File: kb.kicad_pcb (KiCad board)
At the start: 2 copper layers, 110.5 x 91.4 mm, 67 parts, among them U4 HOLE

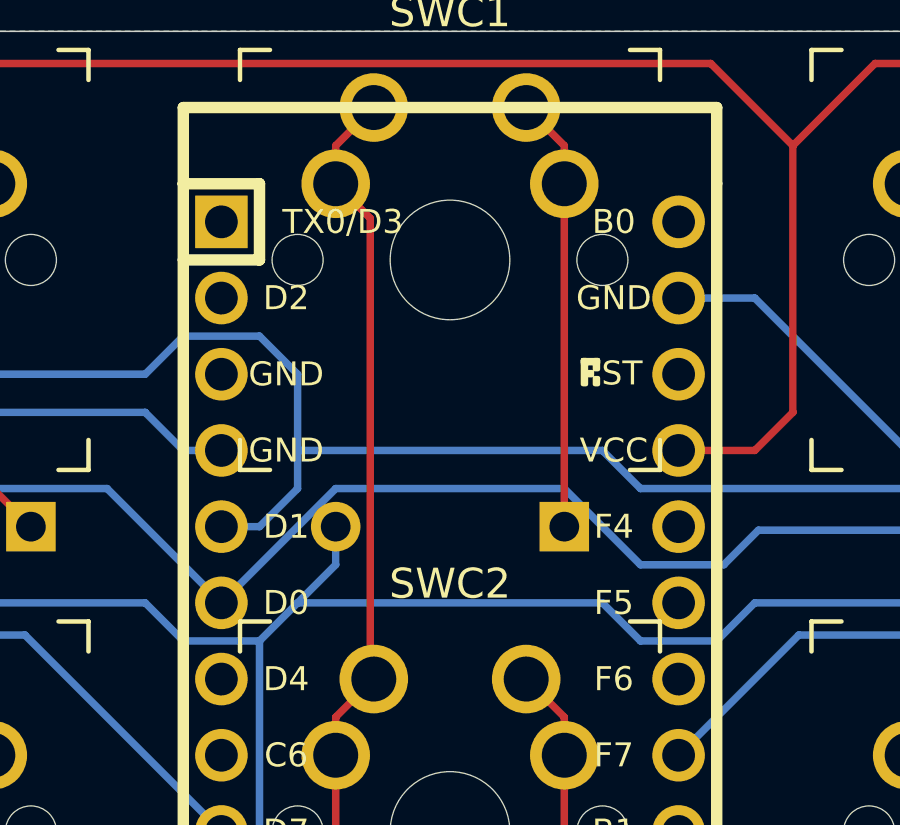
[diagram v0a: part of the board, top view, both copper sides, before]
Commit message: Fixed intersecting diode and trace (fixed #1)
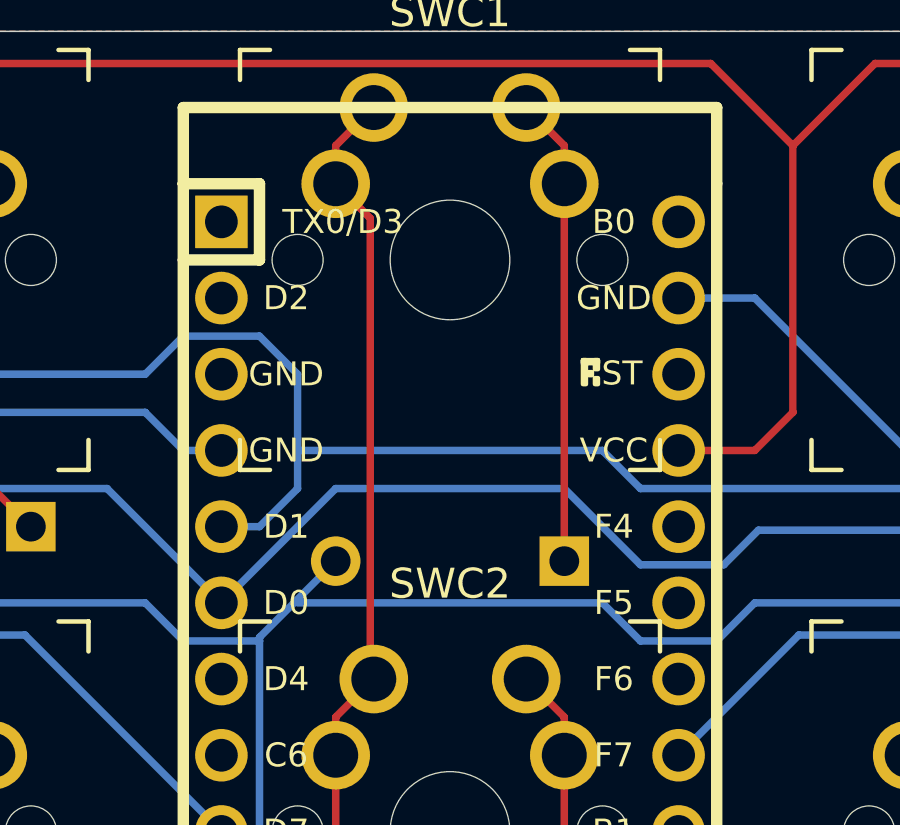
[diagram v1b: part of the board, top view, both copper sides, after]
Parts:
- moved D11 1.15 mm to (135.9, 71.0)
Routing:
- net Net-(D11-Pad2): track 14.5 -> 15.6 mm
- net Net-(D1-Pad1): track 120.3 -> 119.2 mm

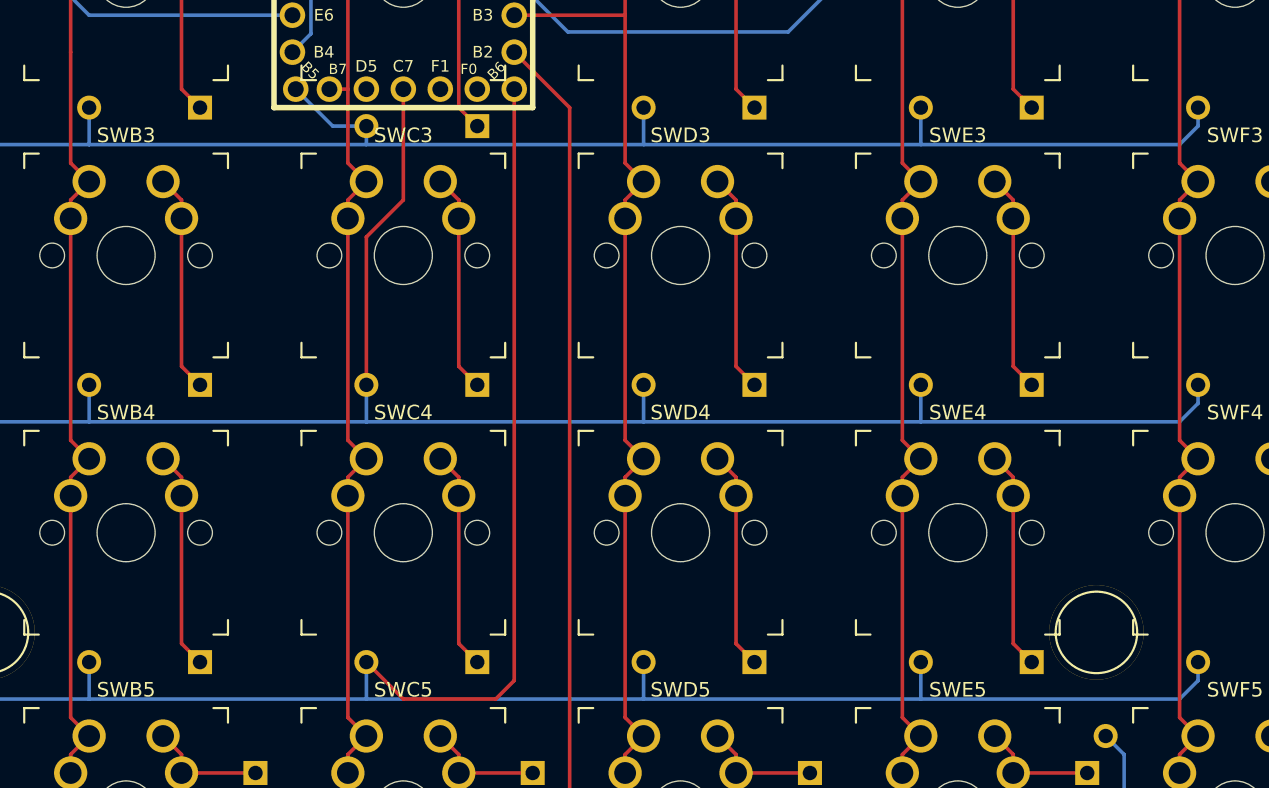
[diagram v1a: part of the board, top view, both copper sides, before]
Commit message: Shifted diode to improve fill
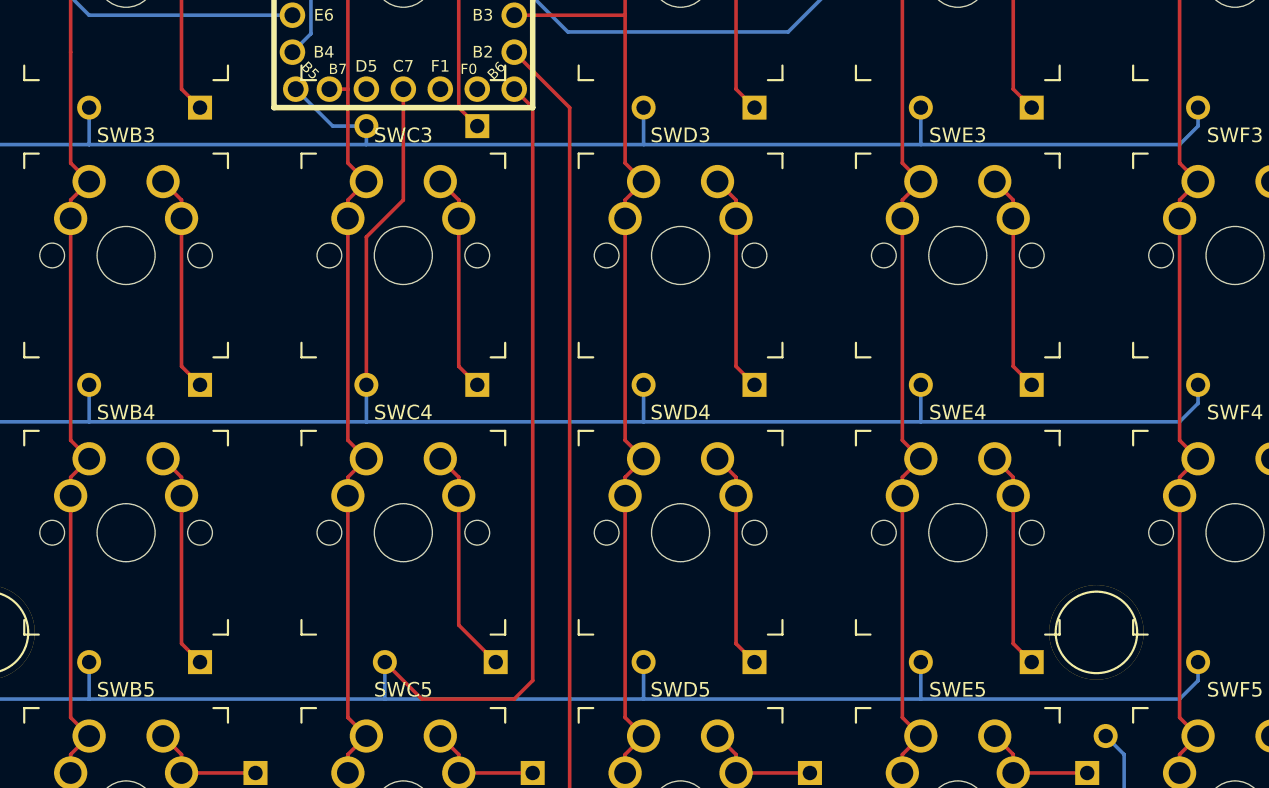
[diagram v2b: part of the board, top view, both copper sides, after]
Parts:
- moved D14 1.27 mm to (138.4, 127.0)
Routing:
- net Net-(D14-Pad2): track 15.0 -> 15.5 mm
- net Net-(D14-Pad1): track 161.4 -> 161.9 mm

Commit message: Improved fill (fixed #2)
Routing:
- net Net-(UL1-Pad1): track 67.3 -> 0.00 mm
- net Net-(UL1-Pad3): track 90.5 -> 102.5 mm
- net Net-(UL1-Pad4): track 97.0 -> 87.2 mm

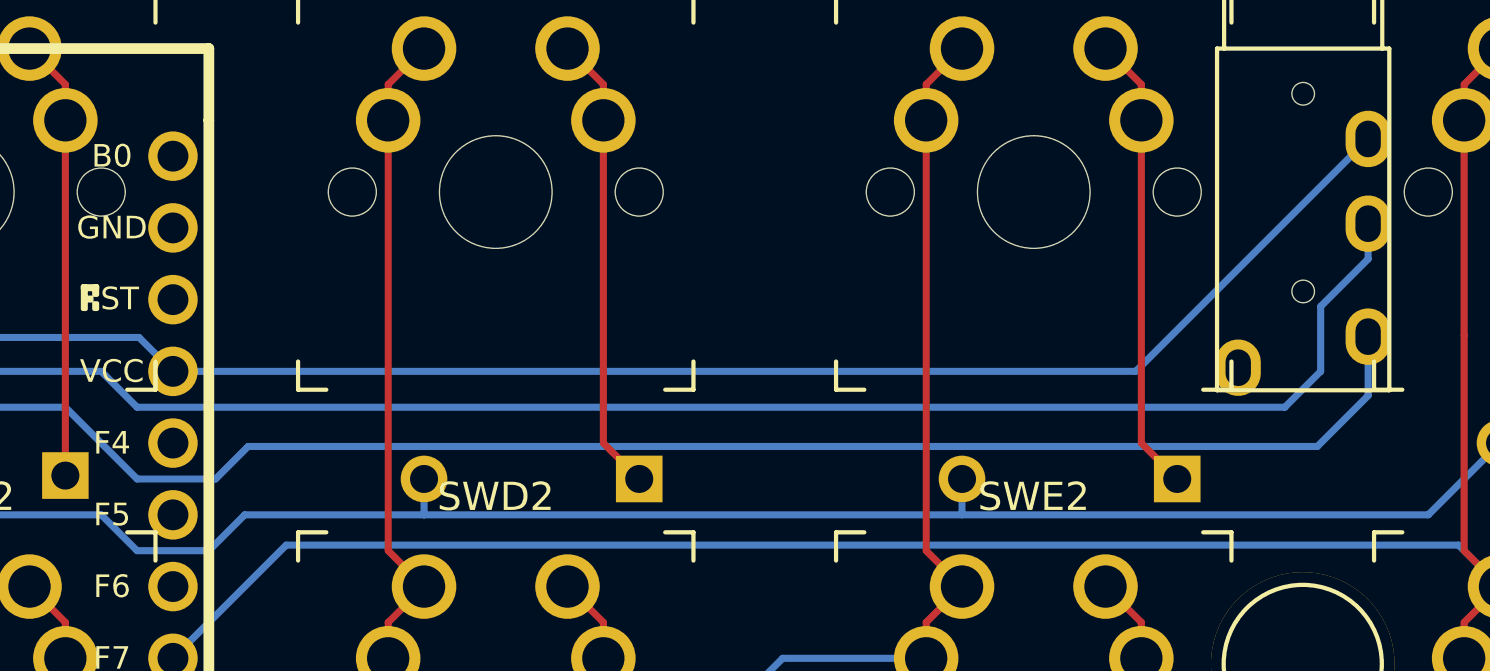
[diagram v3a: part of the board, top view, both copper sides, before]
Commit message: Added pull up resistors for I2C
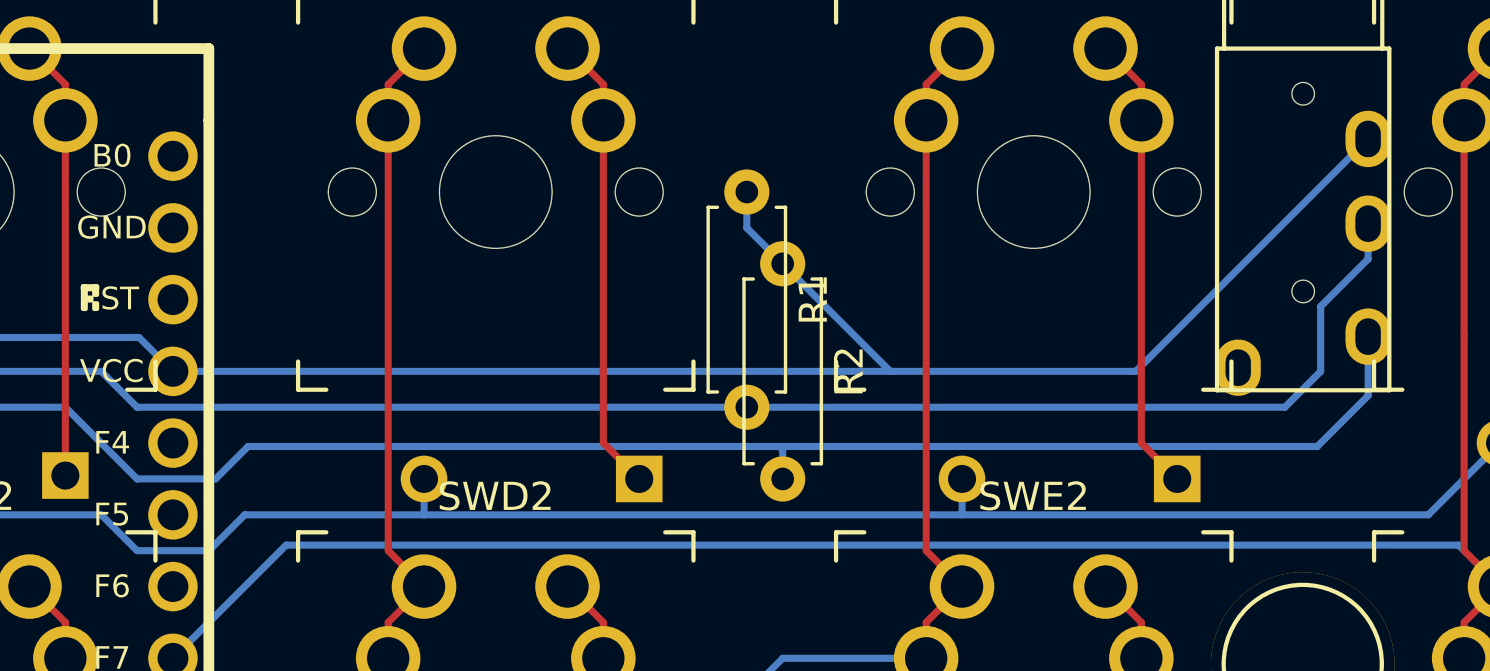
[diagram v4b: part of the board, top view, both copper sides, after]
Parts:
- added R1: 4.7k, Resistor_THT:R_Axial_DIN0207_L6.3mm_D2.5mm_P7.62mm_Horizontal, F.Cu at (163.8, 61.0)
- added R2: 4.7k, Resistor_THT:R_Axial_DIN0207_L6.3mm_D2.5mm_P7.62mm_Horizontal, F.Cu at (165.1, 63.5)
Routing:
- net Net-(R1-Pad1): track 87.2 -> 95.7 mm
- net Net-(R2-Pad2): track 85.6 -> 86.8 mm

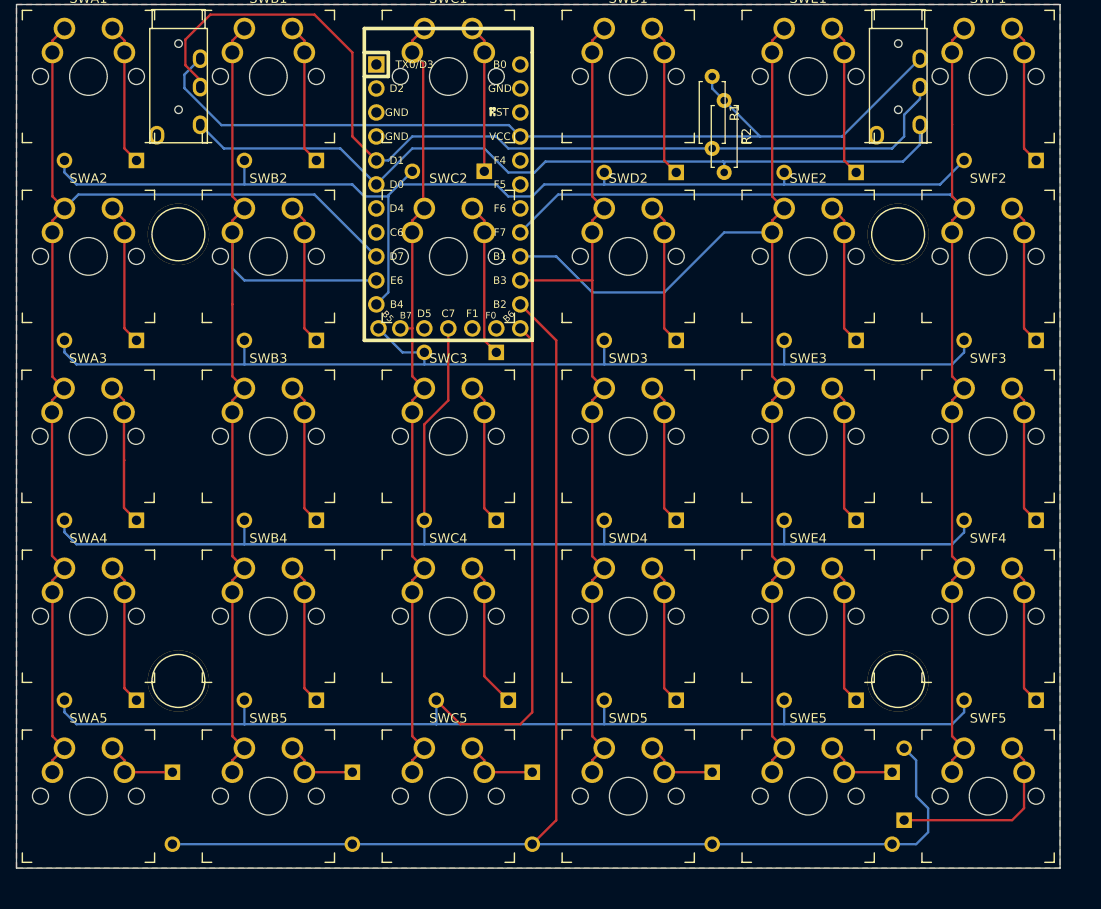
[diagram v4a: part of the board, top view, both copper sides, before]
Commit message: Fixed diode orientation (#3), added bridge points for left/right board, and other cleanup
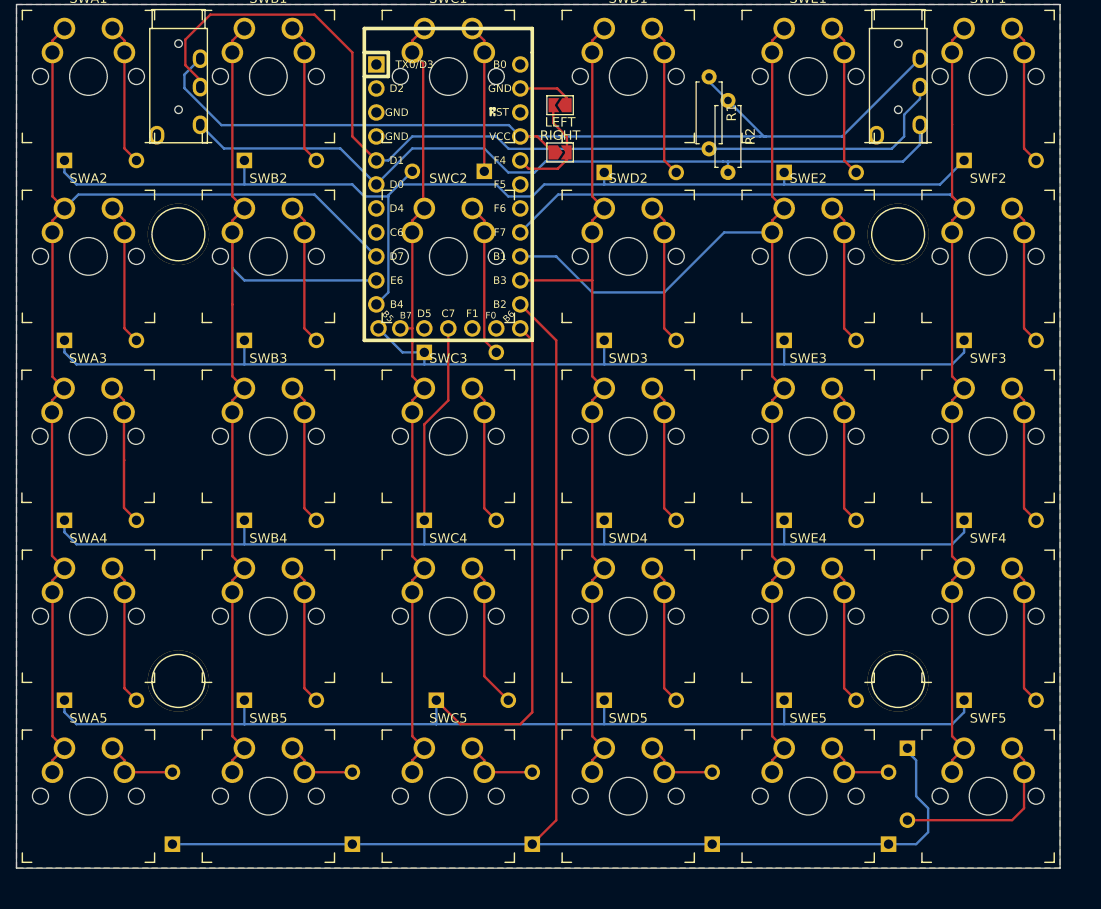
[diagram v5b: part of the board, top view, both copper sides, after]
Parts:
- added LEFT: LEFT, Jumper:SolderJumper-2_P1.3mm_Open_TrianglePad1.0x1.5mm, F.Cu at (147.7, 64.0)
- added RIGHT: RIGHT, Jumper:SolderJumper-2_P1.3mm_Open_TrianglePad1.0x1.5mm, F.Cu at (147.7, 69.0)
- D1, D10, D11, D12, D13, D14, D15, D16, D17, D18, D19, D2, D20, D21, D22, D23, D24, D25, D26, D27, D28, D29, D3, D30, D4, D5, D6, D7, D8, D9: footprint Keebio-Parts:Diode -> footprints:Diode
- moved R2 0.40 mm to (165.5, 63.5)
- moved D25 0.38 mm to (182.5, 138.4), turned to -90 degrees
- moved D30 0.35 mm to (184.5, 135.9), turned to 90 degrees
- moved R1 0.33 mm to (163.5, 61.0)
- turned D1 to 180 degrees
- turned D10 to -90 degrees
- turned D12 to 180 degrees
- turned D13 to 180 degrees
- turned D14 to 180 degrees
- turned D15 to -90 degrees
- turned D16 to 180 degrees
- turned D17 to 180 degrees
- turned D18 to 180 degrees
- turned D19 to 180 degrees
- turned D2 to 180 degrees
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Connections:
- UMC1 pad 1: Net-(UMC1-Pad1) -> unconnected-(UMC1-TX0/PD3-Pad1)
- UMC1 pad 18: Net-(UMC1-Pad18) -> unconnected-(UMC1-A1/PF6-Pad18)
- UMC1 pad 19: Net-(UMC1-Pad19) -> unconnected-(UMC1-A2/PF5-Pad19)
- UMC1 pad 2: Net-(UMC1-Pad2) -> unconnected-(UMC1-RX1/PD2-Pad2)
- UMC1 pad 22: Net-(UMC1-Pad22) -> unconnected-(UMC1-RST-Pad22)
- UMC1 pad 24: Net-(UMC1-Pad24) -> unconnected-(UMC1-B0-Pad24)
- UMC1 pad 26: Net-(UMC1-Pad26) -> unconnected-(UMC1-D5-Pad26)
- UMC1 pad 28: Net-(UMC1-Pad28) -> unconnected-(UMC1-F1-Pad28)
- UMC1 pad 29: Net-(UMC1-Pad29) -> unconnected-(UMC1-F0-Pad29)
- UMC1 pad 7: Net-(UMC1-Pad7) -> unconnected-(UMC1-4/PD4-Pad7)
- UMC1 pad 8: Net-(UMC1-Pad8) -> unconnected-(UMC1-5/PC6-Pad8)
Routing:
- net Net-(UMC1-A3/PF4): track 0.00 -> 12.1 mm
- net Net-(UL1-SLEEVE): track 0.00 -> 6.12 mm
- net Net-(UL1-RING2): track 95.7 -> 100.3 mm
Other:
- net class Default removed

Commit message: Silkscreen tweaks
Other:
- board text added: "2025-08-12"
- board text added: "LiamBoard revB"
- board text added: "fruzyna.net"
